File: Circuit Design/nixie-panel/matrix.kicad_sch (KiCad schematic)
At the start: 144 parts

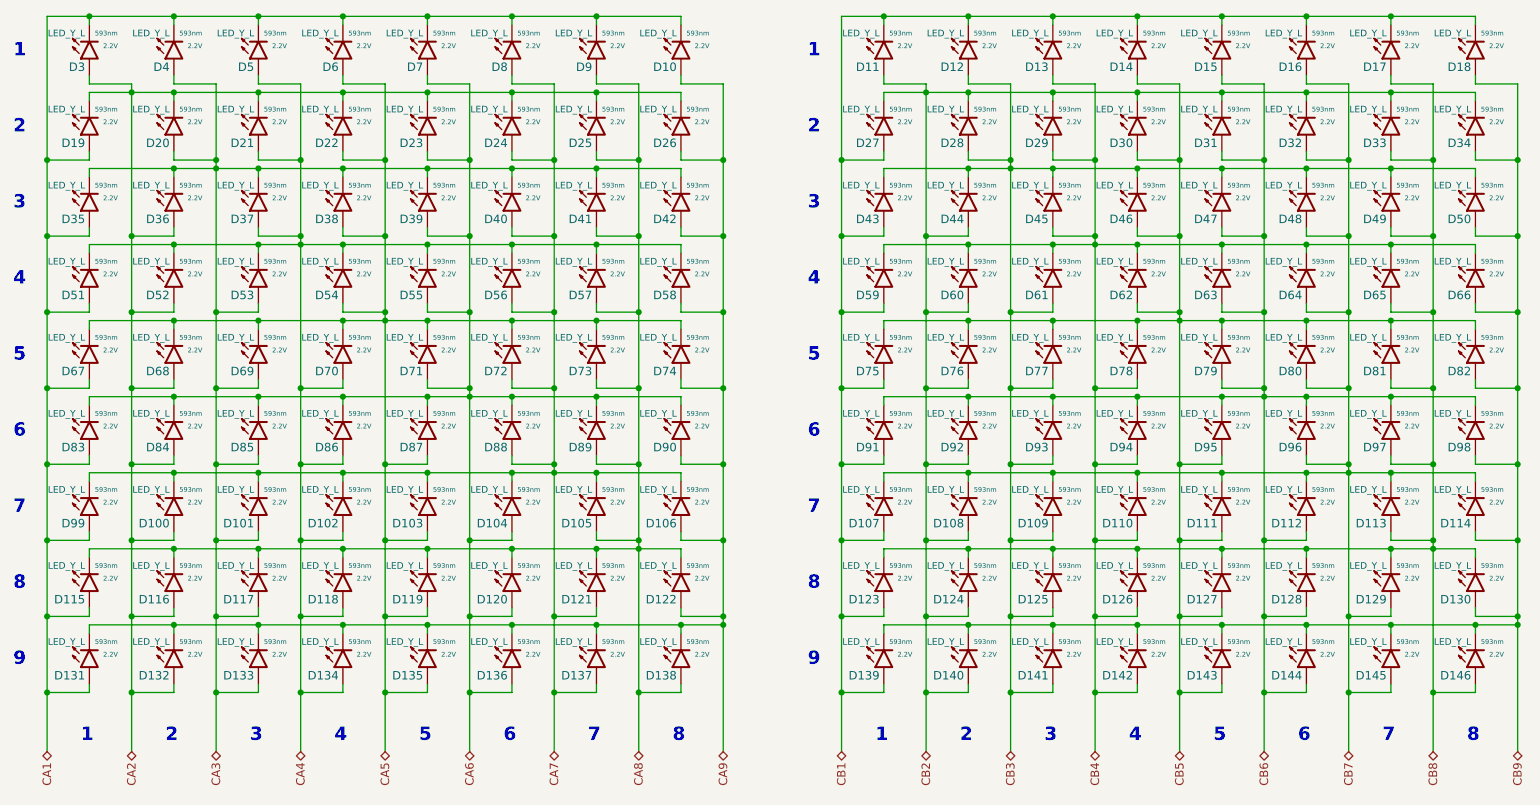
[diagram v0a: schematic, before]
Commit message: created two individual enzyme submodules for each circuit project
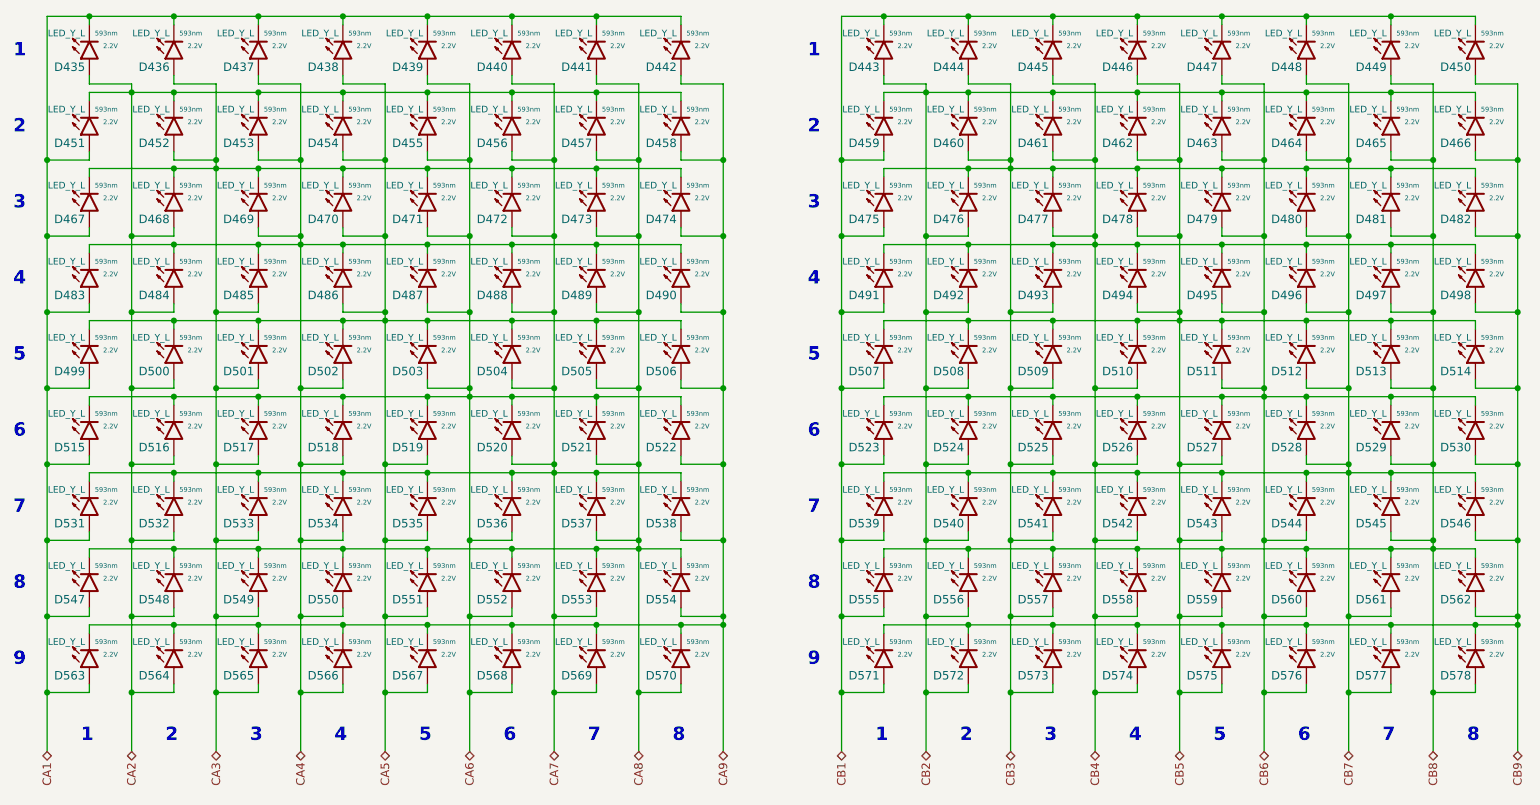
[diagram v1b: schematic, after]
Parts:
- renumbered D3 to D435, D4 to D436, D5 to D437, D6 to D438, D7 to D439, D8 to D440, D9 to D441, D10 to D442, D11 to D443, D12 to D444, D13 to D445, D14 to D446, D15 to D447, D16 to D448, D17 to D449, D18 to D450, D19 to D451, D20 to D452, D21 to D453, D22 to D454, D23 to D455, D24 to D456, D25 to D457, D26 to D458, D27 to D459, D28 to D460, D29 to D461, D30 to D462, D31 to D463, D32 to D464, D33 to D465, D34 to D466, D35 to D467, D36 to D468, D37 to D469, D38 to D470, D39 to D471, D40 to D472, D41 to D473, D42 to D474, D43 to D475, D44 to D476, D45 to D477, D46 to D478, D47 to D479, D48 to D480, D49 to D481, D50 to D482, D51 to D483, D52 to D484, D53 to D485, D54 to D486, D55 to D487, D56 to D488, D57 to D489, D58 to D490, D59 to D491, D60 to D492, D61 to D493, D62 to D494, D63 to D495, D64 to D496, D65 to D497, D66 to D498, D67 to D499, D68 to D500, D69 to D501, D70 to D502, D71 to D503, D72 to D504, D73 to D505, D74 to D506, D75 to D507, D76 to D508, D77 to D509, D78 to D510, D79 to D511, D80 to D512, D81 to D513, D82 to D514, D83 to D515, D84 to D516, D85 to D517, D86 to D518, D87 to D519, D88 to D520, D89 to D521, D90 to D522, D91 to D523, D92 to D524, D93 to D525, D94 to D526, D95 to D527, D96 to D528, D97 to D529, D98 to D530, D99 to D531, D100 to D532, D101 to D533, D102 to D534, D103 to D535, D104 to D536, D105 to D537, D106 to D538, D107 to D539, D108 to D540, D109 to D541, D110 to D542, D111 to D543, D112 to D544, D113 to D545, D114 to D546, D115 to D547, D116 to D548, D117 to D549, D118 to D550, D119 to D551, D120 to D552, D121 to D553, D122 to D554, D123 to D555, D124 to D556, D125 to D557, D126 to D558, D127 to D559, D128 to D560, D129 to D561, D130 to D562, D131 to D563, D132 to D564, D133 to D565, D134 to D566, D135 to D567, D136 to D568, D137 to D569, D138 to D570, D139 to D571, D140 to D572, D141 to D573, D142 to D574, D143 to D575, D144 to D576, D145 to D577, D146 to D578
